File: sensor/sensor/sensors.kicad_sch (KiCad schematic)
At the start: 12 parts, among them U3 APDS-9960

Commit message: imu
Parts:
- removed R12, R13: 4.7k, symbol Device:R
- added C10, C7: 0.1u, symbol Device:C
- added C8: 2.2u, symbol Device:C
- added C9: 10n, symbol Device:C
- added R19: 4.7k, symbol Device:R
- added U6: ICM-20602, Package_LGA:LGA-16_3x3mm_P0.5mm_LayoutBorder3x5y, symbol Sensor_Motion:ICM-20602
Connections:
- net +3.3V: now also R16.1, C7.1, C8.1, C9.1, R19.1, U6.1 (VDDIO), U6.16 (VDD)
- net GND: now also C10.2, C7.2, C8.2, C9.2, U6.10 (GND), U6.11 (GND), U6.12 (GND), U6.13 (GND), U6.15 (GND), U6.4 (SAO/SD0), U6.8 (FSYNC), U6.9 (GND)
- net scl: now also U6.2 (SCL/SPC)
- net sda: now also U6.3 (SDA/SDI)
- net at C4.1, R15.2, U3.8 (VDD): no longer R16.1
- new net: R19.2, U6.5 (~{CS})
- new net: C10.1, U6.14 (REGOUT)
- no-connect marks 0 -> 1
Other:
- note added: "APDS-9960"
- note added: "ICM-20602"
- moved on the sheet: R16

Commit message: updated sensor
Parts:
- added C11: 100n, symbol Device:C
- added C12: 4.7u, symbol Device:C
- added R20, R21: 10k, symbol Device:R
- added R22, R23: 4.7k, symbol Device:R
- added U7: VL53L1CXV0FY1, Sensor_Distance:ST_VL53L1x, symbol Sensor_Distance:VL53L1CXV0FY1
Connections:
- net +3.3V: now also C11.1, C12.1, R20.1, R21.1, R22.1, R23.1, U7.1 (AVDDVCSEL), U7.11 (AVDD)
- net GND: now also C11.2, C12.2, U7.12 (GND), U7.2 (AVSSVCSEL), U7.3 (GND), U7.4 (GND), U7.6 (GND)
- net scl: now also R23.2, U7.10 (SCL)
- net sda: now also R22.2, U7.9 (SDA)
- new net: R21.2, U7.5 (XSHUT)
- new net: R20.2, U7.7 (GPIO1)
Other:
- note added: "VL53L1X"

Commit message: karmanyaah's footprints
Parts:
- added J4, J5, J6, J7: Conn_01x03_Socket, Connector_PinSocket_2.54mm:PinSocket_1x03_P2.54mm_Vertical, symbol Connector:Conn_01x03_Socket
- added U8: PCA9536D, symbol Interface_Expansion:PCA9536D
- C10, C11, C12, C4, C5, C6, C7, C8, C9: footprint (none) -> Capacitor_SMD:C_0603_1608Metric_Pad1.08x0.95mm_HandSolder
- D1, D2: footprint (none) -> LED_SMD:LED_0805_2012Metric_Pad1.15x1.40mm_HandSolder
- R15, R16, R17, R18, R19, R20, R21, R22, R23: footprint (none) -> Resistor_SMD:R_0603_1608Metric_Pad0.98x0.95mm_HandSolder
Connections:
- net +3.3V: now also J4.2 (Pin_2), J5.2 (Pin_2), J6.2 (Pin_2), J7.2 (Pin_2), U8.8 (VDD)
- net GND: now also J4.1 (Pin_1), J5.1 (Pin_1), J6.1 (Pin_1), J7.1 (Pin_1), U8.4 (VSS)
- net scl: now also U8.6 (SCL)
- net sda: now also U8.7 (SDA)
- new net: J5.3 (Pin_3), U8.2 (IO1)
- new net: J4.3 (Pin_3), U8.1 (IO0)
- new net: J6.3 (Pin_3), U8.3 (IO2)
- new net: J7.3 (Pin_3), U8.5 (IO3)
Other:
- note added: "TCA9636DGKR"

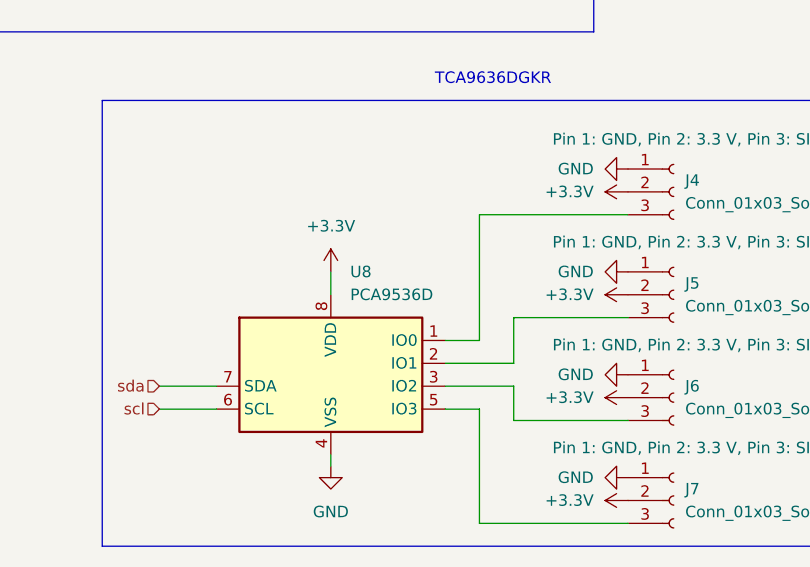
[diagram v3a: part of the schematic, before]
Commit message: new tca9536 footprint
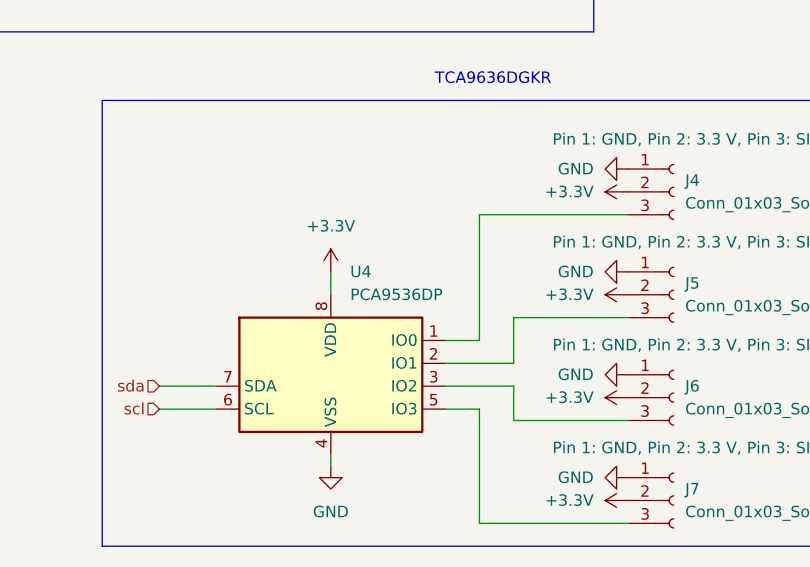
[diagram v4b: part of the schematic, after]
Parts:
- removed U8: PCA9536D, symbol Interface_Expansion:PCA9536D
- added U4: PCA9536DP, Package_SO:TSSOP-8_3x3mm_P0.65mm, symbol Interface_Expansion:PCA9536DP
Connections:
- net +3.3V: now also U4.8 (VDD)
- net GND: now also U4.4 (VSS)
- net scl: now also U4.6 (SCL)
- net sda: now also U4.7 (SDA)
- net at J5.3 (Pin_3): now also U4.2 (IO1)
- net at J4.3 (Pin_3): now also U4.1 (IO0)
- net at J6.3 (Pin_3): now also U4.3 (IO2)
- net at J7.3 (Pin_3): now also U4.5 (IO3)
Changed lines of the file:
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@@
-	)
-	(symbol
-		(lib_id "Interface_Expansion:PCA9536D")
-		(at 203.2 137.16 0)
-		(unit 1)
-		(exclude_from_sim no)
-		(in_bom yes)
-		(on_board yes)
-		(dnp no)
-		(fields_autoplaced yes)
-		(property "Reference" "U8"
-			(at 205.3433 127 0)
-			(effects
-				(font
-					(size 1.27 1.27)
-				)
-				(justify left)
-			)
-		)
-		(property "Value" "PCA9536D"
-			(at 205.3433 129.54 0)
-			(effects
-				(font
-					(size 1.27 1.27)
-				)
-				(justify left)
-			)
-		)
-		(property "Footprint" ""
-			(at 228.6 146.05 0)
-			(effects
-				(font
-					(size 1.27 1.27)
-				)
-				(hide yes)
-			)
-		)
-		(property "Datasheet" "http://www.nxp.com/docs/en/data-sheet/PCA9536.pdf"
-			(at 198.12 180.34 0)
-			(effects
-				(font
-					(size 1.27 1.27)
-				)
-				(hide yes)
-			)
-		)
-		(property "Description" "4-bit I2C-bus and SMBus IO port, SOIC-8"
-			(at 203.2 137.16 0)
-			(effects
-				(font
-					(size 1.27 1.27)
-				)
-				(hide yes)
-			)
-		)
-		(pin "2"
-		)
-		(pin "6"
-		)
-		(pin "7"
-		)
-		(pin "8"
-		)
-		(pin "1"
-		)
-		(pin "5"
-		)
-		(pin "4"
-		)
-		(pin "3"
-		)
-		(instances
-			(project "sensor"
-				(path "/46f6a130-b02e-4523-867c-7812ad0e1543/5749ed06-df97-48a5-a63f-8384a2d309d9"
-					(reference "U8")
-					(unit 1)
-				)
-			)
-		)
 	)
 	(symbol
@@
 	)
 	(symbol
+		(lib_id "Interface_Expansion:PCA9536DP")
+		(at 203.2 137.16 0)
+		(unit 1)
+		(exclude_from_sim no)
+		(in_bom yes)
+		(on_board yes)
+		(dnp no)
+		(fields_autoplaced yes)
+		(property "Reference" "U4"
+			(at 205.3433 127 0)
+			(effects
+				(font
+					(size 1.27 1.27)
+				)
+				(justify left)
+			)
+		)
+		(property "Value" "PCA9536DP"
+			(at 205.3433 129.54 0)
+			(effects
+				(font
+					(size 1.27 1.27)
+				)
+				(justify left)
+			)
+		)
+		(property "Footprint" "Package_SO:TSSOP-8_3x3mm_P0.65mm"
+			(at 228.6 146.05 0)
+			(effects
+				(font
+					(size 1.27 1.27)
+				)
+				(hide yes)
+			)
+		)
+		(property "Datasheet" "http://www.nxp.com/docs/en/data-sheet/PCA9536.pdf"
+			(at 198.12 180.34 0)
+			(effects
+				(font
+					(size 1.27 1.27)
+				)
+				(hide yes)
+			)
+		)
+		(property "Description" "4-bit I2C-bus and SMBus IO port, TSSOP-8"
+			(at 203.2 137.16 0)
+			(effects
+				(font
+					(size 1.27 1.27)
+				)
+				(hide yes)
+			)
+		)
+		(pin "4"
+		)
+		(pin "6"
+		)
+		(pin "2"
+		)
+		(pin "3"
+		)
+		(pin "1"
+		)
+		(pin "5"
+		)
+		(pin "7"
+		)
+		(pin "8"
+		)
+		(instances
+			(project ""
+				(path "/46f6a130-b02e-4523-867c-7812ad0e1543/5749ed06-df97-48a5-a63f-8384a2d309d9"
+					(reference "U4")
+					(unit 1)
+				)
+			)
+		)
+	)
+	(symbol
 		(lib_id "power:+3.3V")
 		(at 38.1 74.93 0)
@@
 		(on_board yes)
 		(dnp no)
-		(fields_autoplaced yes)
 		(property "Reference" "R17"
 			(at 63.5 54.61 90)

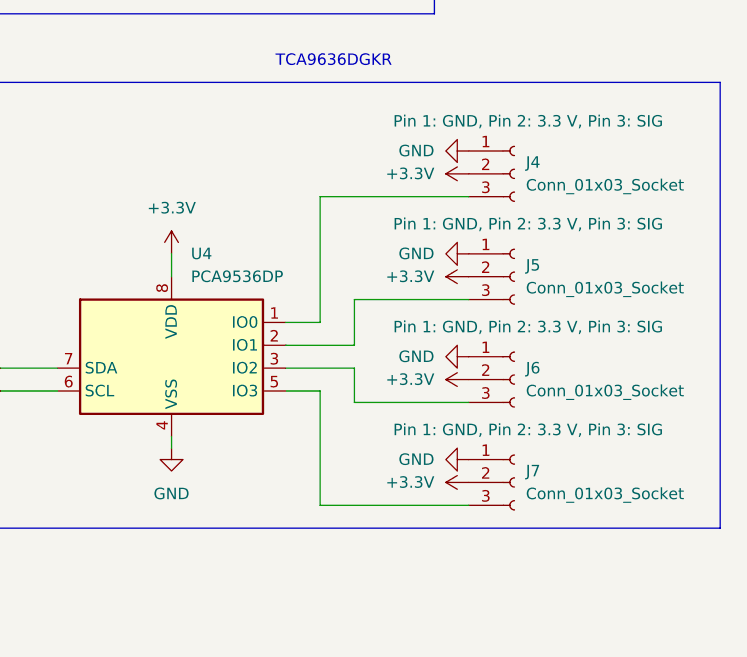
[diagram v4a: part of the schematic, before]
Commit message: began wiring PCB
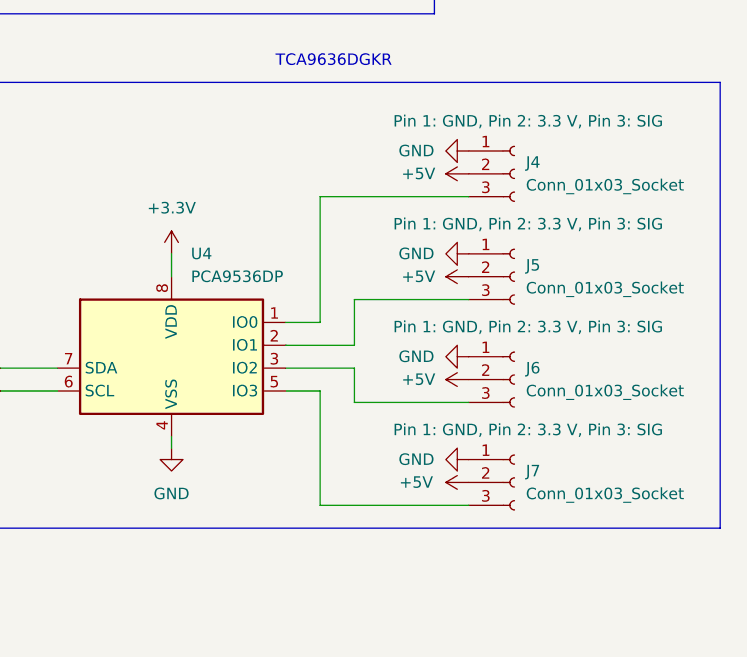
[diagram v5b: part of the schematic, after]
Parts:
- C10, C11, C7, C9: footprint Capacitor_SMD:C_0603_1608Metric_Pad1.08x0.95mm_HandSolder -> Capacitor_SMD:C_0402_1005Metric_Pad0.74x0.62mm_HandSolder
- R15, R16, R17, R18, R19, R20, R21, R22, R23: footprint Resistor_SMD:R_0603_1608Metric_Pad0.98x0.95mm_HandSolder -> Resistor_SMD:R_0402_1005Metric_Pad0.72x0.64mm_HandSolder
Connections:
- net +3.3V: no longer J4.2 (Pin_2), J5.2 (Pin_2), J6.2 (Pin_2), J7.2 (Pin_2)
- net +5V: now also J4.2 (Pin_2), J5.2 (Pin_2), J6.2 (Pin_2), J7.2 (Pin_2)
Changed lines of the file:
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@@
 			)
 		)
-		(property "Footprint" "Resistor_SMD:R_0603_1608Metric_Pad0.98x0.95mm_HandSolder"
+		(property "Footprint" "Resistor_SMD:R_0402_1005Metric_Pad0.72x0.64mm_HandSolder"
 			(at 157.48 176.022 90)
 			(effects
@@
 			)
 		)
-		(property "Footprint" "Capacitor_SMD:C_0603_1608Metric_Pad1.08x0.95mm_HandSolder"
+		(property "Footprint" "Capacitor_SMD:C_0402_1005Metric_Pad0.74x0.62mm_HandSolder"
 			(at 86.6648 149.86 0)
 			(effects
@@
 		(on_board yes)
 		(dnp no)
-		(fields_autoplaced yes)
 		(property "Reference" "#PWR039"
 			(at 240.03 140.97 0)
@@
 			)
 		)
-		(property "Value" "+3.3V"
-			(at 232.41 140.9699 90)
-			(effects
-				(font
-					(size 1.27 1.27)
-				)
-				(justify left)
+		(property "Value" "+5V"
+			(at 230.632 140.97 90)
+			(effects
+				(font
+					(size 1.27 1.27)
+				)
 			)
 		)
@@
 			)
 		)
-		(property "Footprint" "Resistor_SMD:R_0603_1608Metric_Pad0.98x0.95mm_HandSolder"
+		(property "Footprint" "Resistor_SMD:R_0402_1005Metric_Pad0.72x0.64mm_HandSolder"
 			(at 157.48 163.322 90)
 			(effects
@@
 		(on_board yes)
 		(dnp no)
-		(fields_autoplaced yes)
 		(property "Reference" "#PWR041"
 			(at 240.03 152.4 0)
@@
 			)
 		)
-		(property "Value" "+3.3V"
-			(at 232.41 152.3999 90)
-			(effects
-				(font
-					(size 1.27 1.27)
-				)
-				(justify left)
+		(property "Value" "+5V"
+			(at 230.378 152.4 90)
+			(effects
+				(font
+					(size 1.27 1.27)
+				)
 			)
 		)
@@
 			)
 		)
-		(property "Footprint" "Capacitor_SMD:C_0603_1608Metric_Pad1.08x0.95mm_HandSolder"
+		(property "Footprint" "Capacitor_SMD:C_0402_1005Metric_Pad0.74x0.62mm_HandSolder"
 			(at 168.6052 43.18 0)
 			(effects
@@
 		(on_board yes)
 		(dnp no)
-		(fields_autoplaced yes)
 		(property "Reference" "#PWR037"
 			(at 240.03 129.54 0)
@@
 			)
 		)
-		(property "Value" "+3.3V"
-			(at 232.41 129.5399 90)
-			(effects
-				(font
-					(size 1.27 1.27)
-				)
-				(justify left)
+		(property "Value" "+5V"
+			(at 230.632 129.54 90)
+			(effects
+				(font
+					(size 1.27 1.27)
+				)
 			)
 		)
@@
 			)
 		)
-		(property "Footprint" "Resistor_SMD:R_0603_1608Metric_Pad0.98x0.95mm_HandSolder"
+		(property "Footprint" "Resistor_SMD:R_0402_1005Metric_Pad0.72x0.64mm_HandSolder"
 			(at 62.23 48.768 90)
 			(effects
@@
 		(on_board yes)
 		(dnp no)
-		(fields_autoplaced yes)
 		(property "Reference" "#PWR035"
 			(at 240.03 118.11 0)
@@
 			)
 		)
-		(property "Value" "+3.3V"
-			(at 232.41 118.1099 90)
-			(effects
-				(font
-					(size 1.27 1.27)
-				)
-				(justify left)
+		(property "Value" "+5V"
+			(at 230.632 118.11 90)
+			(effects
+				(font
+					(size 1.27 1.27)
+				)
 			)
 		)
@@
 			)
 		)
-		(property "Footprint" "Resistor_SMD:R_0603_1608Metric_Pad0.98x0.95mm_HandSolder"
+		(property "Footprint" "Resistor_SMD:R_0402_1005Metric_Pad0.72x0.64mm_HandSolder"
 			(at 55.118 156.21 90)
 			(effects
@@
 			)
 		)
-		(property "Footprint" "Resistor_SMD:R_0603_1608Metric_Pad0.98x0.95mm_HandSolder"
+		(property "Footprint" "Resistor_SMD:R_0402_1005Metric_Pad0.72x0.64mm_HandSolder"
 			(at 179.578 78.74 90)
 			(effects
@@
 			)
 		)
-		(property "Footprint" "Resistor_SMD:R_0603_1608Metric_Pad0.98x0.95mm_HandSolder"
+		(property "Footprint" "Resistor_SMD:R_0402_1005Metric_Pad0.72x0.64mm_HandSolder"
 			(at 55.88 76.708 90)
 			(effects
@@
 			)
 		)
-		(property "Footprint" "Capacitor_SMD:C_0603_1608Metric_Pad1.08x0.95mm_HandSolder"
+		(property "Footprint" "Capacitor_SMD:C_0402_1005Metric_Pad0.74x0.62mm_HandSolder"
 			(at 213.0552 80.01 0)
 			(effects
@@
 			)
 		)
-		(property "Footprint" "Resistor_SMD:R_0603_1608Metric_Pad0.98x0.95mm_HandSolder"
+		(property "Footprint" "Resistor_SMD:R_0402_1005Metric_Pad0.72x0.64mm_HandSolder"
 			(at 63.5 62.738 90)
 			(effects
@@
 			)
 		)
-		(property "Footprint" "Resistor_SMD:R_0603_1608Metric_Pad0.98x0.95mm_HandSolder"
+		(property "Footprint" "Resistor_SMD:R_0402_1005Metric_Pad0.72x0.64mm_HandSolder"
 			(at 60.198 147.32 90)
 			(effects
@@
 			)
 		)
-		(property "Footprint" "Capacitor_SMD:C_0603_1608Metric_Pad1.08x0.95mm_HandSolder"
+		(property "Footprint" "Capacitor_SMD:C_0402_1005Metric_Pad0.74x0.62mm_HandSolder"
 			(at 163.5252 62.23 0)
 			(effects
@@
 			)
 		)
-		(property "Footprint" "Resistor_SMD:R_0603_1608Metric_Pad0.98x0.95mm_HandSolder"
+		(property "Footprint" "Resistor_SMD:R_0402_1005Metric_Pad0.72x0.64mm_HandSolder"
 			(at 98.552 81.28 90)
 			(effects

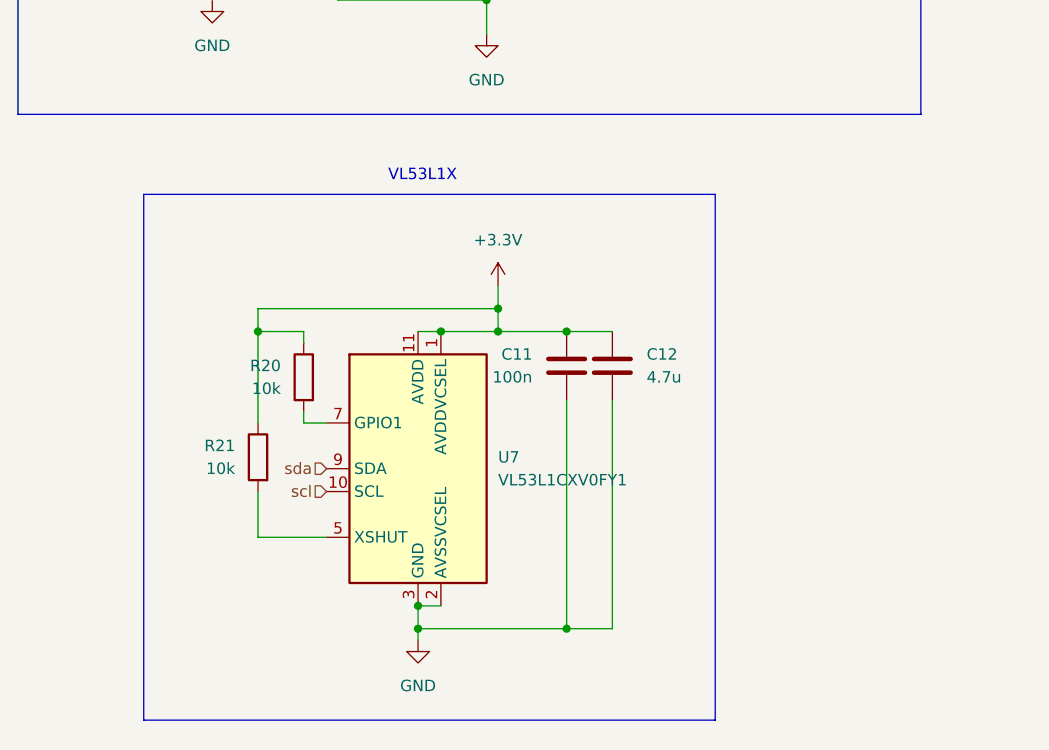
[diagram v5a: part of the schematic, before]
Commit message: new proximity sensor schematic + output RJ12 connectore (pls double check this im just assuming they connect in series)
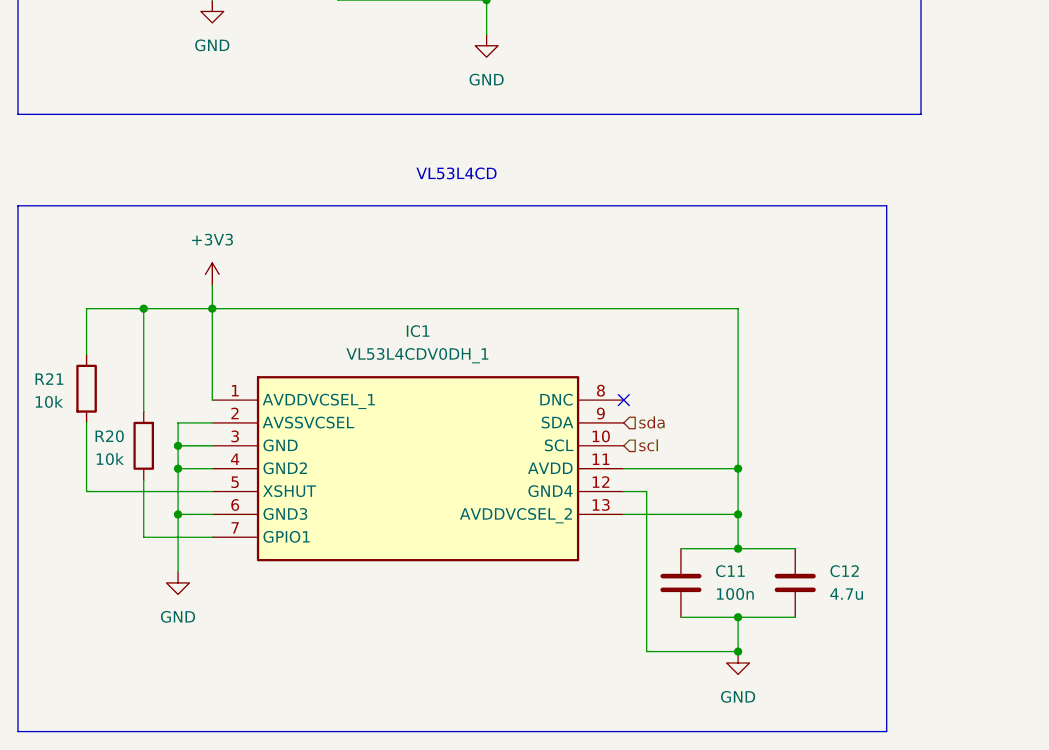
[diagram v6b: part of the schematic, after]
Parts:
- removed U7: VL53L1CXV0FY1, Sensor_Distance:ST_VL53L1x, symbol Sensor_Distance:VL53L1CXV0FY1
- added IC1: VL53L4CDV0DH_1, VL53L4CDV0DH1, symbol VL53L4CDV0DH_1:VL53L4CDV0DH_1
- C11: footprint Capacitor_SMD:C_0402_1005Metric_Pad0.74x0.62mm_HandSolder -> (none)
- C12: footprint Capacitor_SMD:C_0603_1608Metric_Pad1.08x0.95mm_HandSolder -> (none)
- R20, R21: footprint Resistor_SMD:R_0402_1005Metric_Pad0.72x0.64mm_HandSolder -> (none)
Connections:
- net +3.3V: no longer C11.1, C12.1, R20.1, R21.1
- net GND: now also IC1.12 (GND4), IC1.2 (AVSSVCSEL), IC1.3 (GND), IC1.4 (GND2), IC1.6 (GND3)
- net scl: now also IC1.10 (SCL)
- net sda: now also IC1.9 (SDA)
- net at R21.2: now also IC1.5 (XSHUT)
- net +3V3: now reaches R20.2
- net +3V3: now also C11.1, C12.1, R21.1, IC1.1 (AVDDVCSEL_1), IC1.11 (AVDD), IC1.13 (AVDDVCSEL_2)
- new net: IC1.7 (GPIO1), R20.1
- no-connect marks 1 -> 2
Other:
- note added: "VL53L4CD"
- note removed: "VL53L1X"
